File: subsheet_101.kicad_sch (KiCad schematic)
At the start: 8 parts, among them J03 Jumper wire, J04 Jumper wire

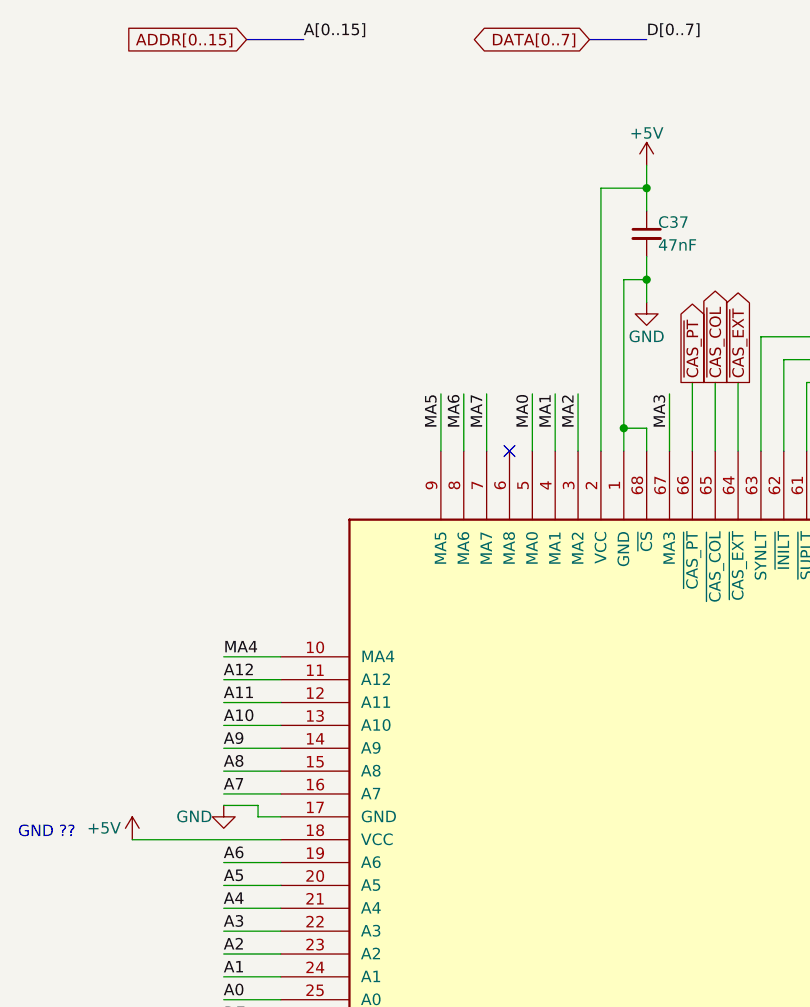
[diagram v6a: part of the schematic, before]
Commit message: Updated gate-array with actual connections (or lack of connections) of some power pins
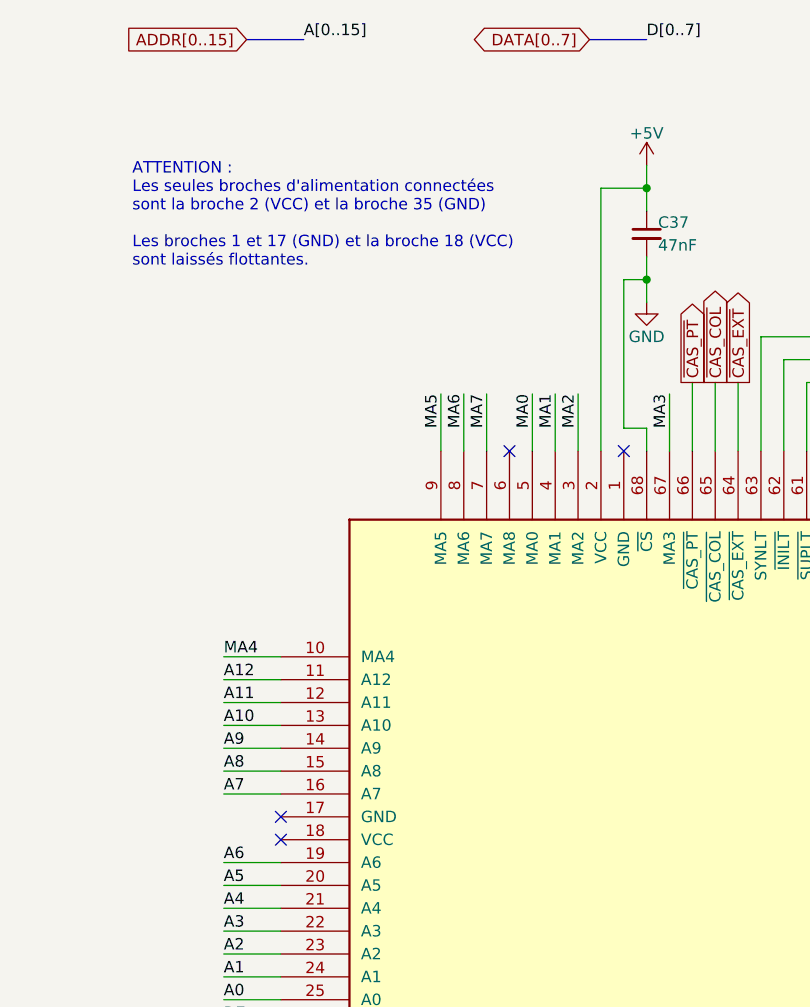
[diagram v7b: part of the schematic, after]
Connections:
- net +5V: no longer I29.18 (VCC)
- net GND: no longer I29.1 (GND), I29.17 (GND)
- no-connect marks 6 -> 9
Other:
- note added: "ATTENTION : Les seules broches d'alimentation connectées sont la broche 2 (VCC) et la broche 35 (GND) Les broches 1 et 17 (GND) et la broche 18 (VCC) sont laissés flottantes."
- note removed: "GND ??"
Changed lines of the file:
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@@
   (junction (at 151.13 101.6) (diameter 0) (color 0 0 0 0)
   )
-  (junction (at 80.01 68.58) (diameter 0) (color 0 0 0 0)
-  )
   (junction (at 82.55 41.91) (diameter 0) (color 0 0 0 0)
   )
+  (no_connect (at 41.91 114.3))
   (no_connect (at 125.73 114.3))
+  (no_connect (at 80.01 71.12))
   (no_connect (at 100.33 157.48))
   (no_connect (at 67.31 71.12))
@@
   (no_connect (at 125.73 96.52))
   (no_connect (at 87.63 157.48))
+  (no_connect (at 41.91 111.76))
   (wire (pts (xy 35.56 93.98) (xy 41.91 93.98))
     (stroke (width 0) (type default))
@@
     (stroke (width 0) (type default))
   )
-  (wire (pts (xy 80.01 68.58) (xy 80.01 71.12))
-    (stroke (width 0) (type default))
-  )
   (wire (pts (xy 143.51 60.96) (xy 140.97 60.96))
     (stroke (width 0) (type default))
@@
     (stroke (width 0) (type default))
   )
-  (wire (pts (xy 25.4 114.3) (xy 41.91 114.3))
-    (stroke (width 0) (type default))
-  )
   (wire (pts (xy 72.39 64.77) (xy 72.39 71.12))
     (stroke (width 0) (type default))
@@
     (stroke (width 0) (type default))
   )
-  (wire (pts (xy 35.56 110.49) (xy 39.37 110.49))
-    (stroke (width 0) (type default))
-  )
   (polyline (pts (xy 195.58 66.04) (xy 135.89 66.04))
     (stroke (width 0) (type default))
@@
     (stroke (width 0) (type default))
   )
-  (wire (pts (xy 39.37 110.49) (xy 39.37 111.76))
-    (stroke (width 0) (type default))
-  )
   (wire (pts (xy 140.97 60.96) (xy 140.97 68.58))
     (stroke (width 0) (type default))
@@
     (stroke (width 0) (type default))
   )
-  (wire (pts (xy 39.37 111.76) (xy 41.91 111.76))
-    (stroke (width 0) (type default))
-  )
   (wire (pts (xy 151.13 101.6) (xy 165.1 101.6))
     (stroke (width 0) (type default))
@@
     (effects (font (size 1.27 1.27)) (justify left bottom))
   )
+  (text "ATTENTION :\nLes seules broches d'alimentation connectées\nsont la broche 2 (VCC) et la broche 35 (GND)\n\nLes broches 1 et 17 (GND) et la broche 18 (VCC)\nsont laissés flottantes."
+    (at 25.4 50.8 0)
+    (effects (font (size 1.27 1.27)) (justify left bottom))
+  )
   (text "Depuis I14" (at 175.26 110.49 0)
-    (effects (font (size 1.27 1.27)) (justify left bottom))
-  )
-  (text "GND ??" (at 12.7 114.3 0)
     (effects (font (size 1.27 1.27)) (justify left bottom))
   )
@@
         (path "/e63e39d7-6ac0-4ffd-8aa3-1841a4541b55/f465a4b1-7c3c-40cc-9e66-ff9f17003d42"
           (reference "#PWR0143") (unit 1)
-        )
-      )
-    )
-  )
-  (symbol (lib_id "power:GND") (at 35.56 110.49 0) (unit 1)
-    (in_bom yes) (on_board yes) (dnp no)
-    (property "Reference" "#PWR0145" (at 35.56 116.84 0)
-      (effects (font (size 1.27 1.27)) hide)
-    )
-    (property "Value" "GND" (at 34.29 111.76 0)
-      (effects (font (size 1.27 1.27)) (justify right))
-    )
-    (property "Footprint" "" (at 35.56 110.49 0)
-      (effects (font (size 1.27 1.27)) hide)
-    )
-    (property "Datasheet" "" (at 35.56 110.49 0)
-      (effects (font (size 1.27 1.27)) hide)
-    )
-    (pin "1")
-    (instances
-      (project "UC-50-001"
-        (path "/e63e39d7-6ac0-4ffd-8aa3-1841a4541b55/f465a4b1-7c3c-40cc-9e66-ff9f17003d42"
-          (reference "#PWR0145") (unit 1)
         )
       )
@@
         )
       )
-    )
-  )
-  (symbol (lib_id "power:+5V") (at 25.4 114.3 0) (unit 1)
-    (in_bom yes) (on_board yes) (dnp no)
-    (property "Reference" "#PWR0146" (at 25.4 118.11 0)
-      (effects (font (size 1.27 1.27)) hide)
-    )
-    (property "Value" "+5V" (at 24.13 113.03 0)
-      (effects (font (size 1.27 1.27)) (justify right))
-    )
-    (property "Footprint" "" (at 25.4 114.3 0)
-      (effects (font (size 1.27 1.27)) hide)
-    )
-    (property "Datasheet" "" (at 25.4 114.3 0)
-      (effects (font (size 1.27 1.27)) hide)
-    )
-    (pin "1")
-    (instances
-      (project "UC-50-001"
-        (path "/e63e39d7-6ac0-4ffd-8aa3-1841a4541b55/f465a4b1-7c3c-40cc-9e66-ff9f17003d42"
-          (reference "#PWR0146") (unit 1)
-        )
-      )

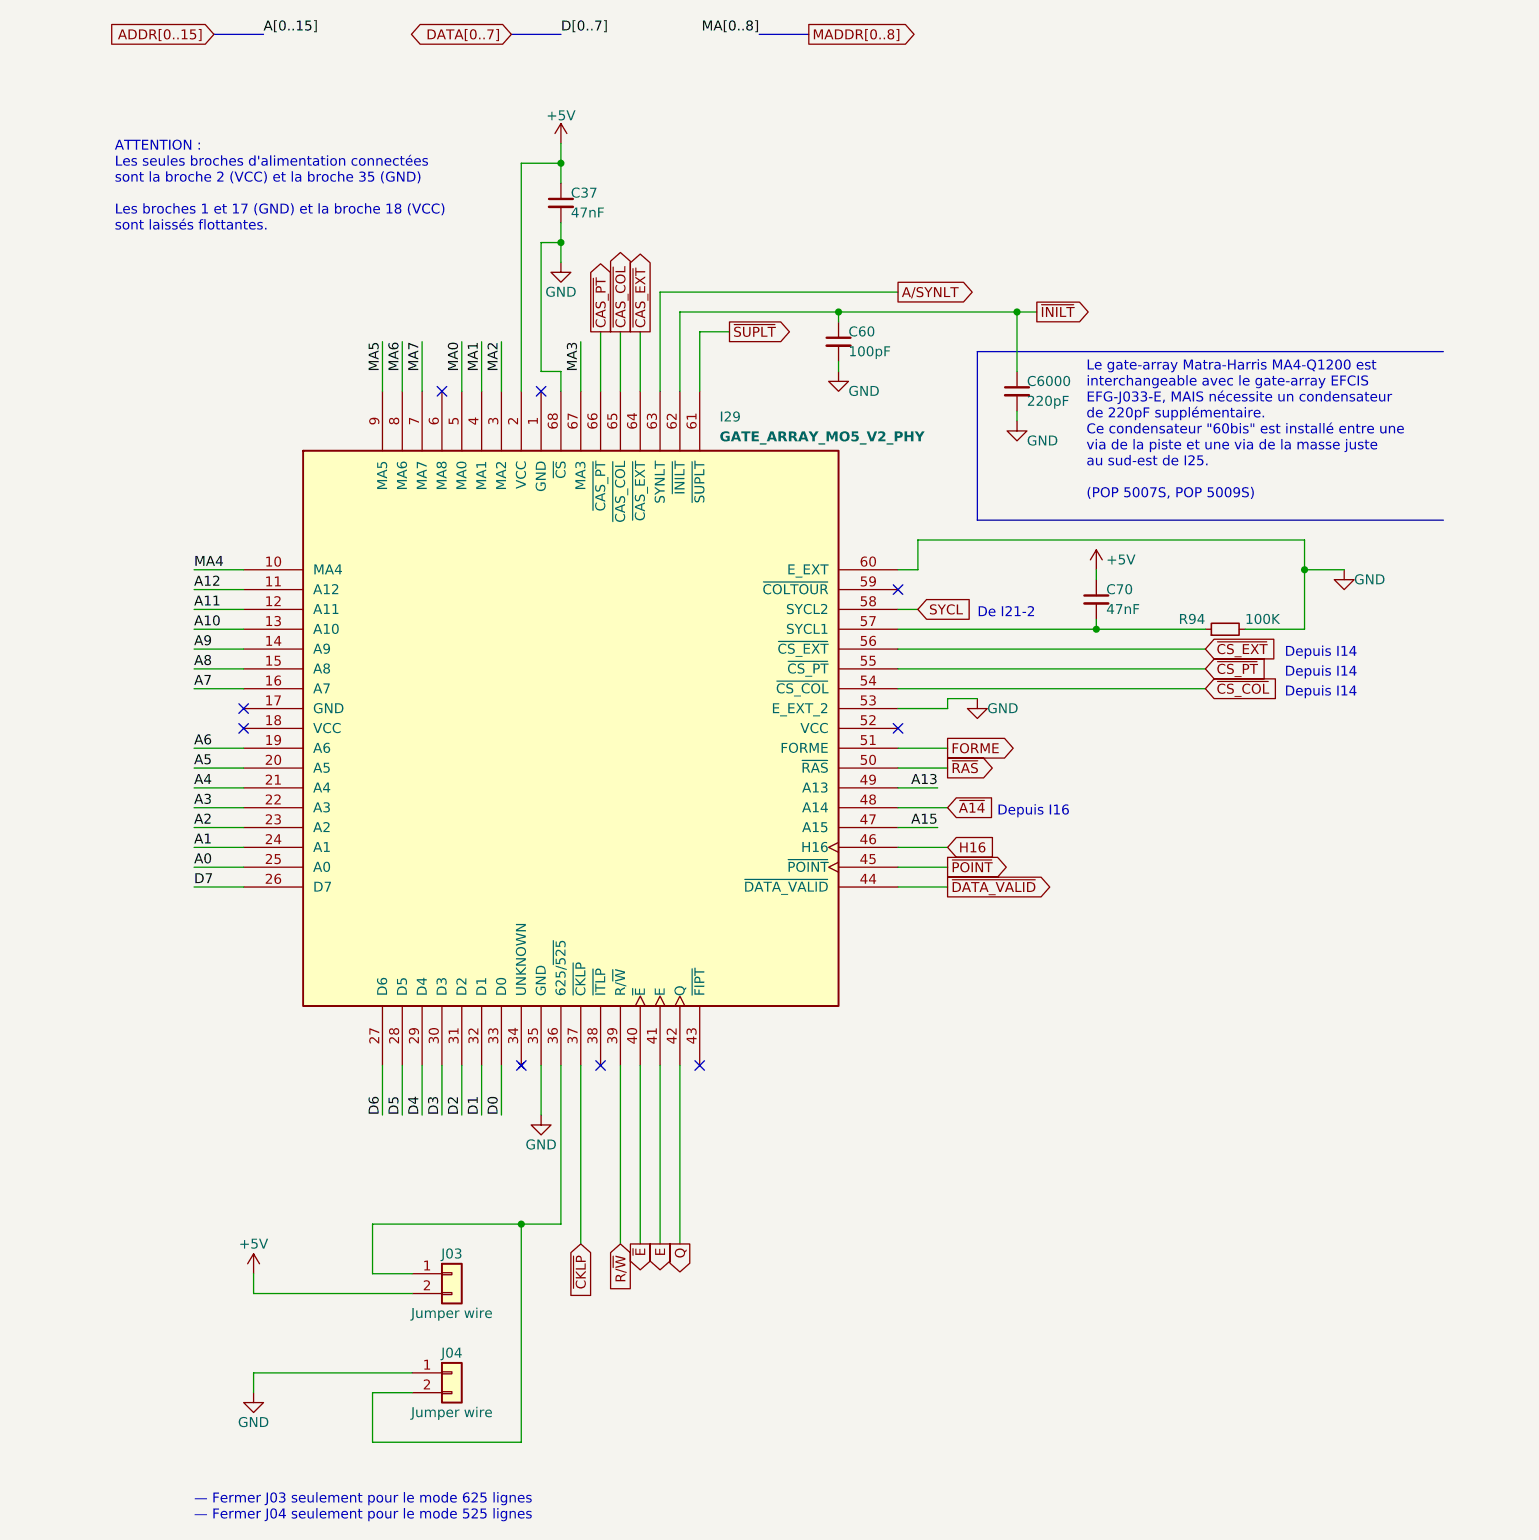
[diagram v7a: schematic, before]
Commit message: more notes on the gate array and not connected power pins
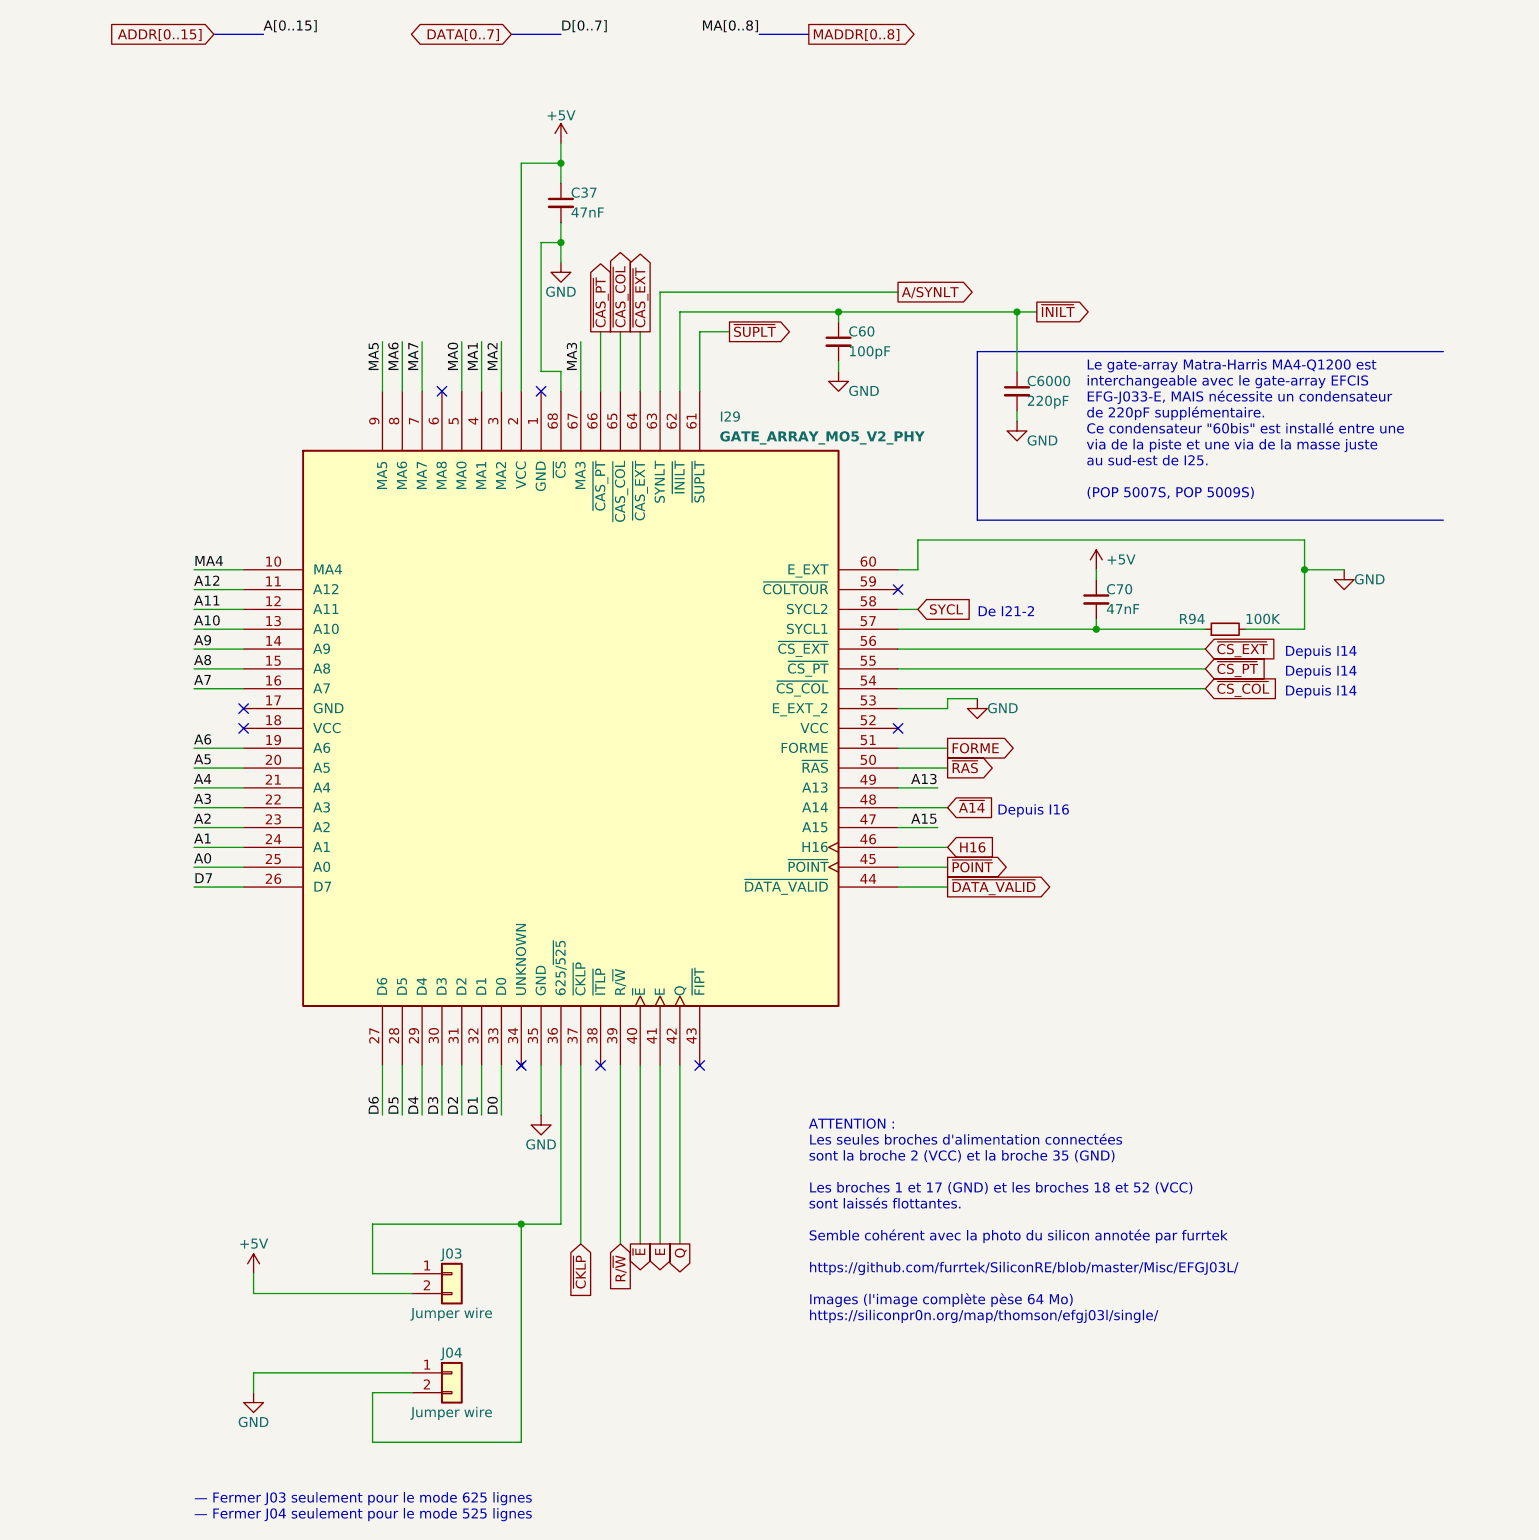
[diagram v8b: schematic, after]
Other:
- note added: "ATTENTION : Les seules broches d'alimentation connectées sont la broche 2 (VCC) et la broche 35 (GND) Les broches 1 et 17 (GND) et les broches 18 et 52 (VCC) sont laissés flottantes. Semble cohérent avec la photo du silicon annotée par furrtek https://github.com/furrtek/SiliconRE/blob/master/Misc/EFGJ03L/ Images (l'image complète pèse 64 Mo) https://siliconpr0n.org/map/thomson/efgj03l/single/"
- note removed: "ATTENTION : Les seules broches d'alimentation connectées sont la broche 2 (VCC) et la broche 35 (GND) Les broches 1 et 17 (GND) et la broche 18 (VCC) sont laissés flottantes."
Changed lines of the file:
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@@
     (effects (font (size 1.27 1.27)) (justify left bottom))
   )
-  (text "ATTENTION :\nLes seules broches d'alimentation connectées\nsont la broche 2 (VCC) et la broche 35 (GND)\n\nLes broches 1 et 17 (GND) et la broche 18 (VCC)\nsont laissés flottantes."
-    (at 25.4 50.8 0)
+  (text "ATTENTION :\nLes seules broches d'alimentation connectées\nsont la broche 2 (VCC) et la broche 35 (GND)\n\nLes broches 1 et 17 (GND) et les broches 18 et 52 (VCC)\nsont laissés flottantes.\n\nSemble cohérent avec la photo du silicon annotée par furrtek\n\nhttps://github.com/furrtek/SiliconRE/blob/master/Misc/EFGJ03L/\n\nImages (l'image complète pèse 64 Mo)\nhttps://siliconpr0n.org/map/thomson/efgj03l/single/\n"
+    (at 114.3 190.5 0)
     (effects (font (size 1.27 1.27)) (justify left bottom))
   )
